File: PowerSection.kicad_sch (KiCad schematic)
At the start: 5 parts, among them J2 USB_B_Micro, U3 TPS62840DLCR

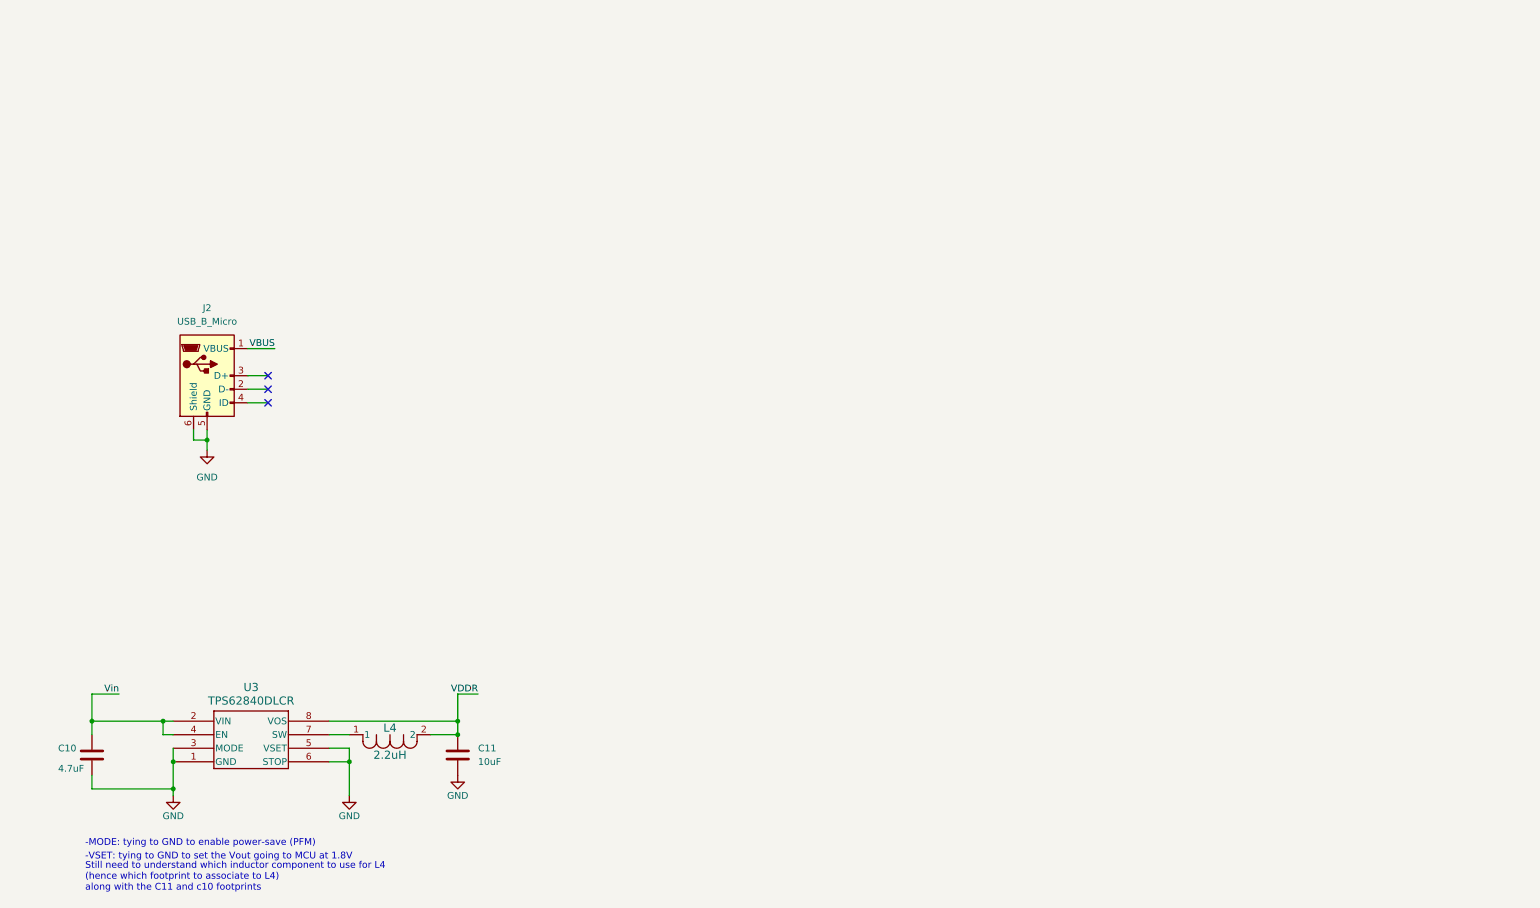
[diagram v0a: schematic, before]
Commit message: done with first version PowerSection of LoTiBloxy plus MCU plus sensor sheets. still have to add meaningfull comments to all schematic components. still have to make sure every symbol is associated to footprint. still have to perform ERC on what implemented.
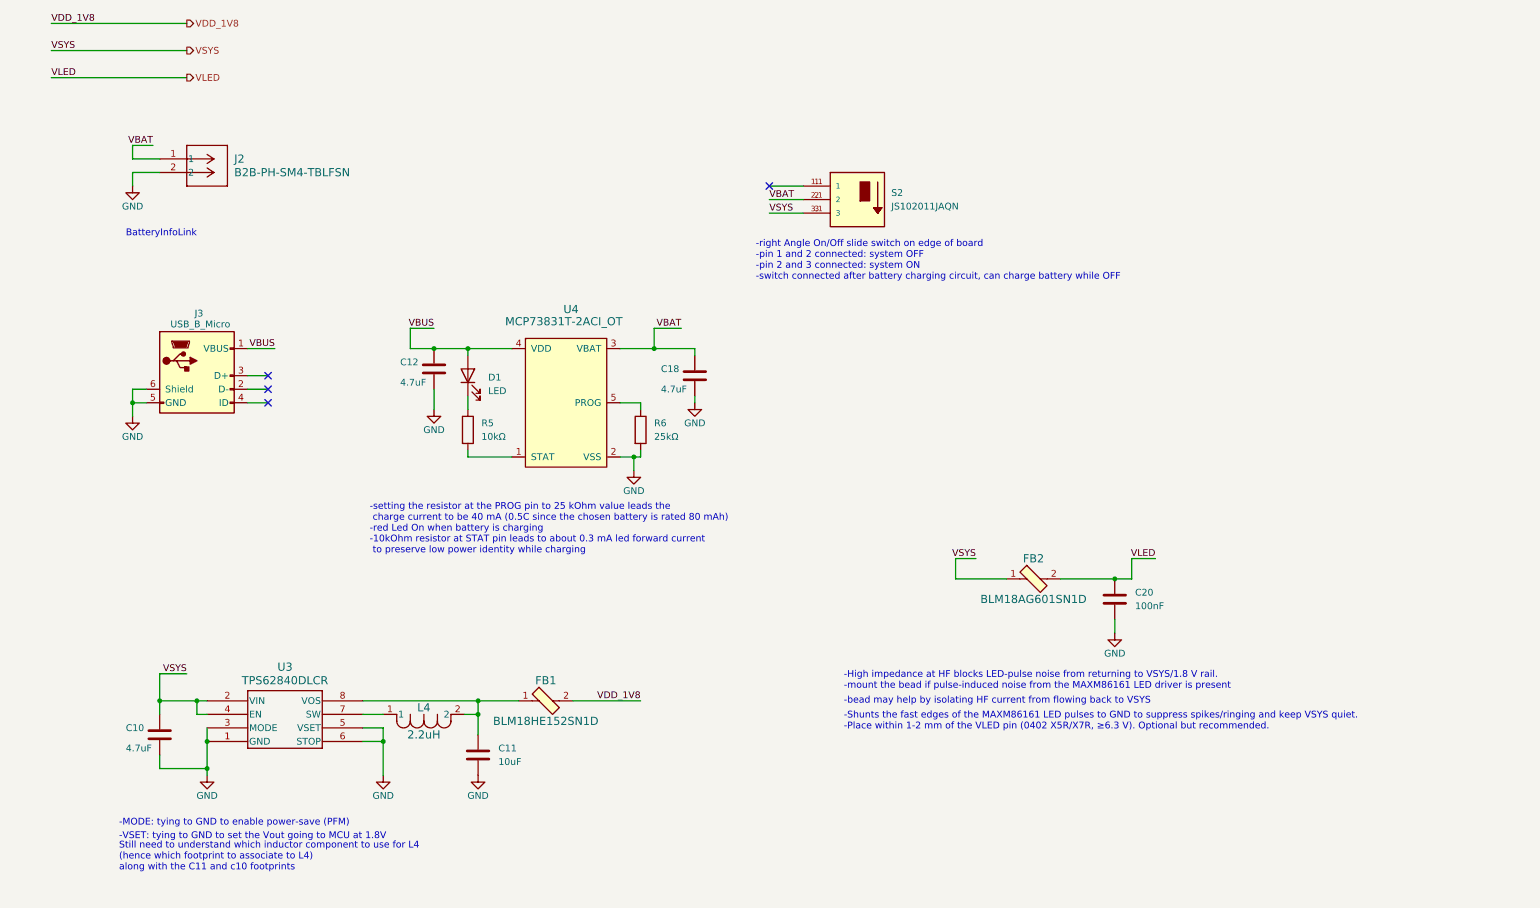
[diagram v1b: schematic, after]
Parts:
- removed J2: USB_B_Micro, ul_microUSB_1051640001_local:CON00906_5_MOL, symbol Connector:USB_B_Micro
- added C12, C18: 4.7uF, symbol unpolarizedcapacitor:C
- added C20: 100nF, symbol unpolarizedcapacitor:C
- added D1: LED, ul_chargingLED_SML_P11UTT86_0402_local:LED_SML-P12UT_ROM, symbol LED_local:LED
- added FB1: BLM18HE152SN1D, digikey-footprints:0603, symbol dk_Ferrite-Beads-and-Chips_local:BLM18HE152SN1D
- added FB2: BLM18AG601SN1D, digikey-footprints:0603, symbol dk_Ferrite-Beads-and-Chips_local:BLM18AG601SN1D
- added J2: B2B-PH-SM4-TBLFSN, ul_BatteryConnector_B2B-PH-SM4-TB-LF-SN_local:CONN_B2B-PH-SM4-TBLFSN_JST, symbol ul_BatteryConnector_B2B-PH-SM4-TB_local:B2B-PH-SM4-TBLFSN
- added J3: USB_B_Micro, ul_microUSB_1051640001_local:CON00906_5_MOL, symbol USB_B_Micro_local:USB_B_Micro
- added R5: 10kΩ, symbol resistor:R
- added R6: 25kΩ, symbol resistor:R
- added S2: JS102011JAQN, rightAngleOnOff_JS102011JAQN_local:SW_JS102011JAQN, symbol rightAngleOnOff_JS102011JAQN_local:JS102011JAQN
- added U4: MCP73831T-2ACI_OT, BatteryCharger_MCP73831T_local:mcp73831T_SOT-23-5, symbol dk_MCP73831BatteryCharger_local:MCP73831T-2ACI_OT
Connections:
- net GND: now also C12.2, C18.2, C20.2, J2.2, J3.5 (GND), J3.6 (Shield), R6.2, U4.2 (VSS)
- net VBUS: now also C12.1, D1.2 (A), J3.1 (VBUS), U4.4 (VDD)
- net VDDR: no longer names the net of C11.1, L4.2, U3.8 (VOS)
- net VDDR: now also FB1.1
- net Vin renamed VSYS
- net VSYS: now also FB2.1, S2.3, S2.3.1 (3)
- new net: R6.1, U4.5 (PROG)
- new net: D1.1 (K), R5.1
- new net: S2.1, S2.1.1 (1)
- new net: R5.2, U4.1 (STAT)
- new net VBAT: C18.1, J2.1, S2.2, S2.2.1 (2), U4.3 (VBAT)
- new net VDD_1V8: FB1.2
- new net VLED: C20.1, FB2.2
- no-connect marks 3 -> 4
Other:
- note added: "-10kOhm resistor at STAT pin leads to about 0.3 mA led forward current to preserve low power identity while charging"
- note added: "-High impedance at HF blocks LED-pulse noise from returning to VSYS/1.8 V rail. -mount the bead if pulse-induced noise from the MAXM86161 LED driver is present"
- note added: "-Shunts the fast edges of the MAXM86161 LED pulses to GND to suppress spikes/ringing and keep VSYS quiet. -Place within 1-2 mm of the VLED pin (0402 X5R/X7R, ≥6.3 V). Optional but recommended."
- note added: "-bead may help by isolating HF current from flowing back to VSYS"
- note added: "-right Angle On/Off slide switch on edge of board -pin 1 and 2 connected: system OFF -pin 2 and 3 connected: system ON -switch connected after battery charging circuit, can charge battery while OFF"
- note added: "-setting the resistor at the PROG pin to 25 kOhm value leads the charge current to be 40 mA (0.5C since the chosen battery is rated 80 mAh) -red Led On when battery is charging"
- note added: "BatteryInfoLink"
- moved on the sheet: C10, C11, L4, U3

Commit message: finished associating each component of each sheet of schematic to relative footprint. filled in first version field for BOM. Provided organized hierechical level directories for all the datasheets for each used component.
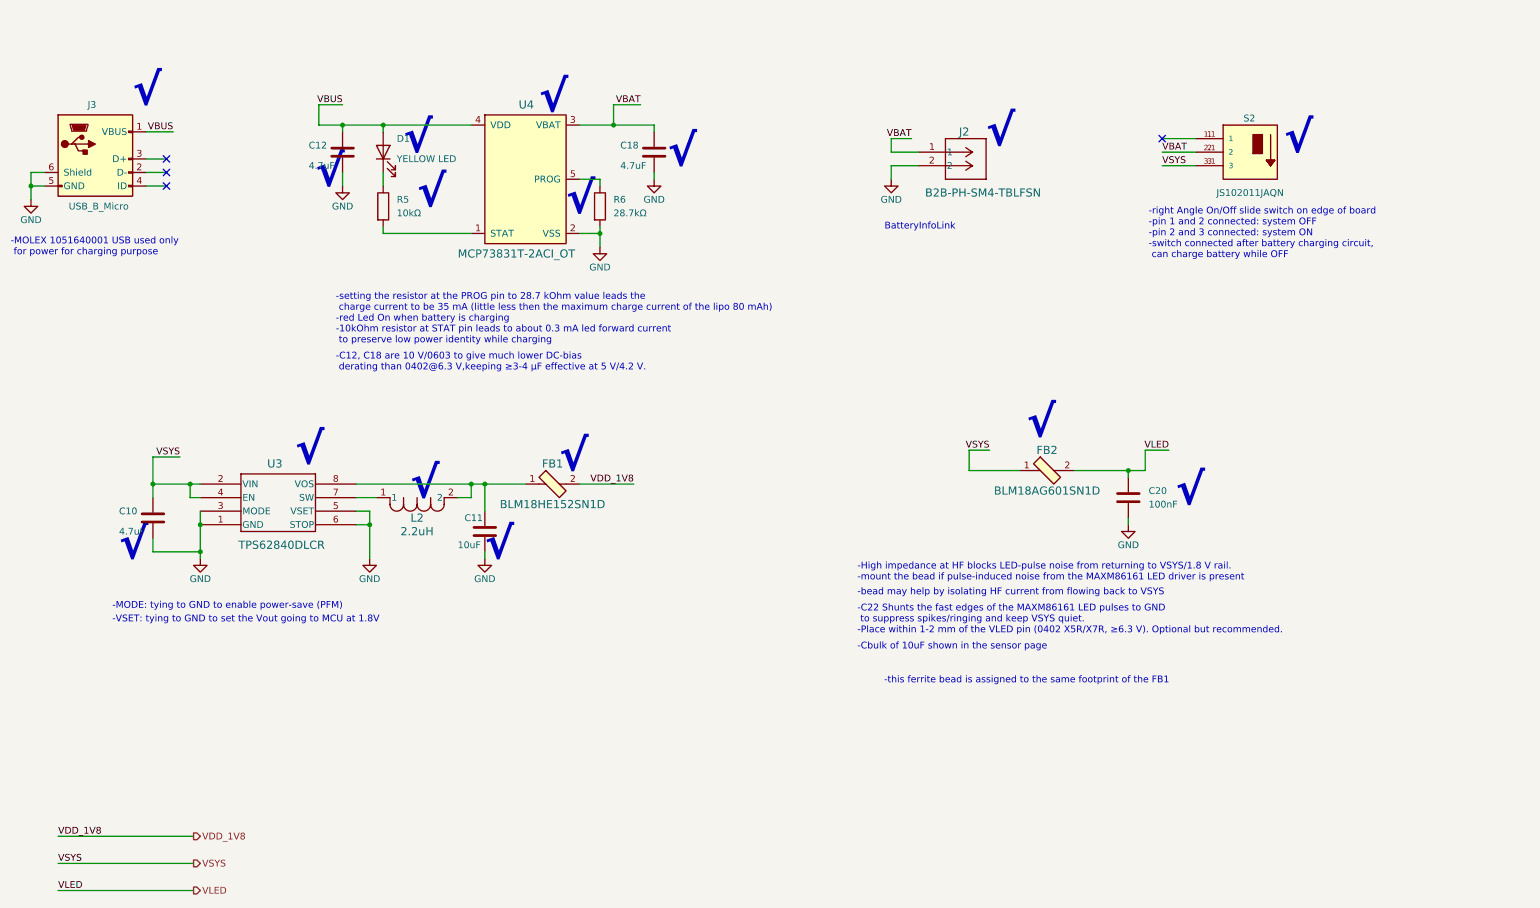
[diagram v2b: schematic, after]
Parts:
- removed L4: 2.2uH, IND_LQG15HN_02_MUR, symbol 15nH_inductor_local:LQG15HS15NJ02D
- added L2: 2.2uH, Inductor_SMD_local:L_0805_2012M_Murata-LQM21PN, symbol inductor_local:LQG15HS2N0S02D
- C10, C12, C18: footprint (none) -> Capacitor_SMD_local:C_0603_1608Metric; MANUFACTURER (none) -> YAGEO; MPN (none) -> CC0603KRX5R6BB475; Package (none) -> 0603; Price (none) -> 0.18; mounting type (none) -> SMD; rohs (none) -> yes; vendor (none) -> DigiKey; vendor part number (none) -> 311-1455-1-ND
- C11: footprint (none) -> Capacitor_SMD_local:C_0603_1608Metric; MANUFACTURER (none) -> Murata Electronics; MPN (none) -> GRM188R60J106ME47D; Package (none) -> 0603; Price (none) -> 0.10; mounting type (none) -> SMD; rohs (none) -> yes; vendor (none) -> DigiKey; vendor part number (none) -> 490-3896-1-ND
- C20: footprint (none) -> Capacitor_SMD_local:C_0402_1005Metric; MANUFACTURER (none) -> Murata Electronics; MPN (none) -> GRM155R70J104KA01D; Package (none) -> 0402; Price (none) -> 0.09; mounting type (none) -> SMD; rohs (none) -> yes; vendor (none) -> DigiKey; vendor part number (none) -> 490-6319-1-ND
- D1: value LED -> YELLOW LED; MANUFACTURER (none) -> Rohm Semiconductor; MPN (none) -> SML-P11YTT86; Package (none) -> 0402; Price (none) -> 0.40; mounting type (none) -> SMD; rohs (none) -> yes; vendor (none) -> DigiKey; vendor part number (none) -> 846-SML-P11YTT86CT-ND
- FB1: footprint digikey-footprints:0603 -> ul_ferriteBead_BLM18HE152SN1D_local:IND_BLM18_0603_MUR; MANUFACTURER (none) -> Murata Electronics; Manufacturer Murata Electronics North America -> Murata Electronics; Package (none) -> 0603; Price (none) -> 0.18; mounting type (none) -> SMD; rohs (none) -> yes; vendor (none) -> DigiKey; vendor part number (none) -> 490-5216-1-ND
- FB2: footprint digikey-footprints:0603 -> ul_ferriteBead_BLM18HE152SN1D_local:IND_BLM18_0603_MUR; MANUFACTURER (none) -> Murata Electronics; Package (none) -> 0603; Price (none) -> 0.09; mounting type (none) -> SMD; rohs (none) -> yes; vendor (none) -> DigiKey; vendor part number (none) -> 490-1014-1-ND
- J2: MANUFACTURER (none) -> JST Sales America Inc.; MPN (none) -> B2B-PH-SM4-TB; Package (none) -> -; Price (none) -> 0.40; mounting type (none) -> SMD; rohs (none) -> yes; vendor (none) -> DigiKey; vendor part number (none) -> 455-B2B-PH-SM4-TBCT-ND
- J3: MANUFACTURER (none) -> Molex; MPN (none) -> 1051640001; Package (none) -> -; Price (none) -> 0.8; mounting type (none) -> SMD, TH; rohs (none) -> yes; vendor (none) -> DigiKey; vendor part number (none) -> WM11263CT-ND
- R5: footprint (none) -> Resistor_SMD_local:R_0402_1005Metric; MANUFACTURER (none) -> Stackpole Electronics Inc; MPN (none) -> RMCF0402FT10K0; Package (none) -> 0402; Price (none) -> 0.09; mounting type (none) -> SMD; rohs (none) -> yes; vendor (none) -> DigiKey; vendor part number (none) -> RMCF0402FT10K0CT-ND
- R6: value 25kΩ -> 28.7kΩ; footprint (none) -> Resistor_SMD_local:R_0402_1005Metric; MANUFACTURER (none) -> Stackpole Electronics Inc; MPN (none) -> RMCF0402FT28K7; Package (none) -> 0402; Price (none) -> 0.09; mounting type (none) -> SMD; rohs (none) -> yes; vendor (none) -> DigiKey; vendor part number (none) -> RMCF0402FT28K7CT-ND
- S2: MPN (none) -> JS102011JAQN; Package None -> -; Price None -> 0.80; mounting type (none) -> SMD; rohs (none) -> yes; vendor (none) -> DigiKey; vendor part number (none) -> CKN10720CT-ND
- U3: footprint VSON8_2P1X1P6_TEX -> ul_buckConv_TPS62840DLCR_local:VSON8_2P1X1P6_TEX; MANUFACTURER (none) -> Texas Instruments; MPN (none) -> TPS62840DLCR; Package (none) -> 8-VFDFN; Price (none) -> 1.79; mounting type (none) -> SMD; rohs (none) -> yes; vendor (none) -> DigiKey; vendor part number (none) -> 296-TPS62840DLCRCT-ND
- U4: MANUFACTURER (none) -> Microchip Technology; Package (none) -> -; Price (none) -> 0.65; mounting type (none) -> SMD; rohs (none) -> yes; vendor (none) -> DigiKey; vendor part number (none) -> MCP73831T-2ACI/OTCT-ND
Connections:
- net at U3.7 (SW): now also L2.1
- net at C11.1, FB1.1, U3.8 (VOS): now also L2.2
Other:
- note added: "-C12, C18 are 10 V/0603 to give much lower DC-bias derating than 0402@6.3 V,keeping ≥3-4 µF effective at 5 V/4.2 V."
- note added: "-C22 Shunts the fast edges of the MAXM86161 LED pulses to GND to suppress spikes/ringing and keep VSYS quiet. -Place within 1-2 mm of the VLED pin (0402 X5R/X7R, ≥6.3 V). Optional but recommended."
- note added: "-Cbulk of 10uF shown in the sensor page"
- note added: "-MOLEX 1051640001 USB used only for power for charging purpose"
- note added: "-setting the resistor at the PROG pin to 28.7 kOhm value leads the charge current to be 35 mA (little less then the maximum charge current of the lipo 80 mAh) -red Led On when battery is charging"
- note added: "-this ferrite bead is assigned to the same footprint of the FB1"
- note added: "√"
- note removed: "-Shunts the fast edges of the MAXM86161 LED pulses to GND to suppress spikes/ringing and keep VSYS quiet. -Place within 1-2 mm of the VLED pin (0402 X5R/X7R, ≥6.3 V). Optional but recommended."
- note removed: "-setting the resistor at the PROG pin to 25 kOhm value leads the charge current to be 40 mA (0.5C since the chosen battery is rated 80 mAh) -red Led On when battery is charging"
- note removed: "Still need to understand which inductor component to use for L4 (hence which footprint to associate to L4) along with the C11 and c10 footprints"
- moved on the sheet: C10, C11, C12, C18, C20, D1, FB1, FB2, J2, J3, R5, R6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

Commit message: ERC step done. most important errors and warnings resolved (the ones about unspecified pins etcetra). with the occasion have done also the checking of the symbols of each component to make sure of correct type of pins.have assigned the different fields related to the first BOM to all the components. need to still assign data sheets and description fields for some components
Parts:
- removed L2: 2.2uH, Inductor_SMD_local:L_0805_2012M_Murata-LQM21PN, symbol inductor_local:LQG15HS2N0S02D
- removed S2: JS102011JAQN, rightAngleOnOff_JS102011JAQN_local:SW_JS102011JAQN, symbol rightAngleOnOff_JS102011JAQN_local:JS102011JAQN
- added L1: 2.2uH, Inductor_SMD_local:L_0805_2012M_Murata-LQM21PN, symbol inductor_local:L
- added S3: JS102011JAQN, rightAngleOnOff_JS102011JAQN_local:SW_JS102011JAQN, symbol rightAngleOnOff_JS102011JAQN_local:JS102011JAQN
- C10, C12, C18, FB1: Price 0.18 -> 0.18 €
- C11: Price 0.10 -> 0.10 €
- C20, FB2, R5, R6: Price 0.09 -> 0.09 €
- D1, J2: Price 0.40 -> 0.40 €
- U3: Price 1.79 -> 1.79 €
- U4: Price 0.65 -> 0.65 €
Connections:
- net GND: now also U3.4 (EN); no longer U3.3 (MODE)
- net VBAT: now also S3.2, S3.2.1 (2)
- net VSYS: now also U3.3 (MODE), S3.3, S3.3.1 (3); no longer U3.4 (EN)
- net SW: now reaches U3.7 (SW)
- net SW: now also L1.1
- net VOS: now reaches C11.1, FB1.1, U3.8 (VOS)
- net VOS: now also L1.2
- net PROG: now reaches R6.1, U4.5 (PROG)
- net STAT: now reaches R5.2, U4.1 (STAT)
- new net: S3.1, S3.1.1 (1)
- no-connect marks 4 -> 3
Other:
- moved on the sheet: C11, FB1, J3
